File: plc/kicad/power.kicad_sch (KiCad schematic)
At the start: 67 parts, among them Q5 BSS138LT1G, Q6 CSD19537Q3, SW3 TSD003B08026A03, U11 LMR16006XDDCR, U12 TPS54560DDAR, U13 TPS26630RGER, U17 TLV76733DRVR

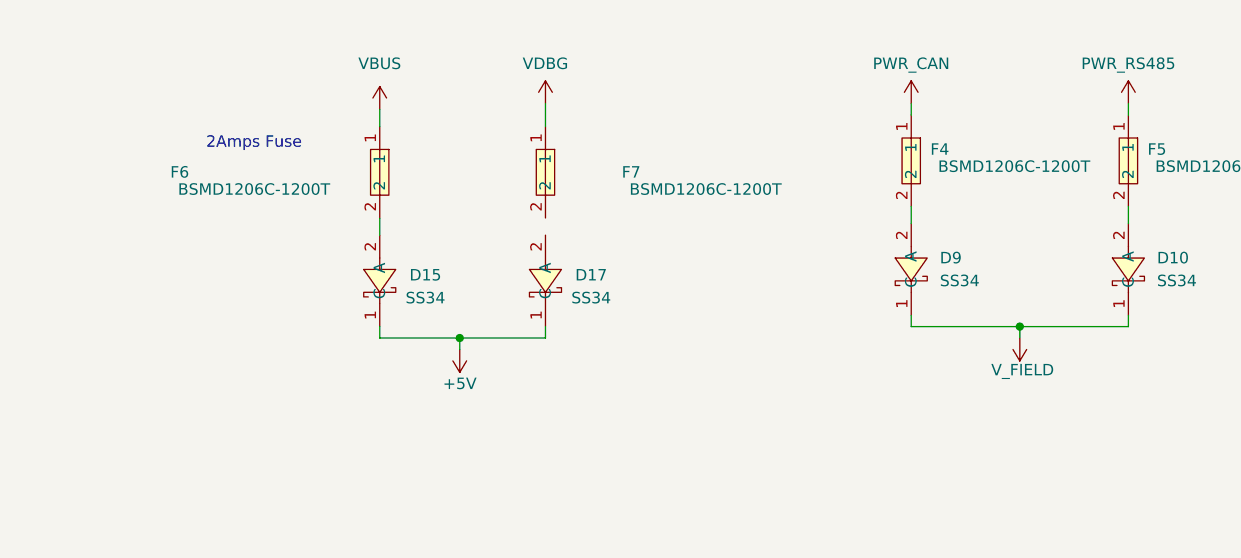
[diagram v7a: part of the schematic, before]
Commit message: AHT20 sensor added
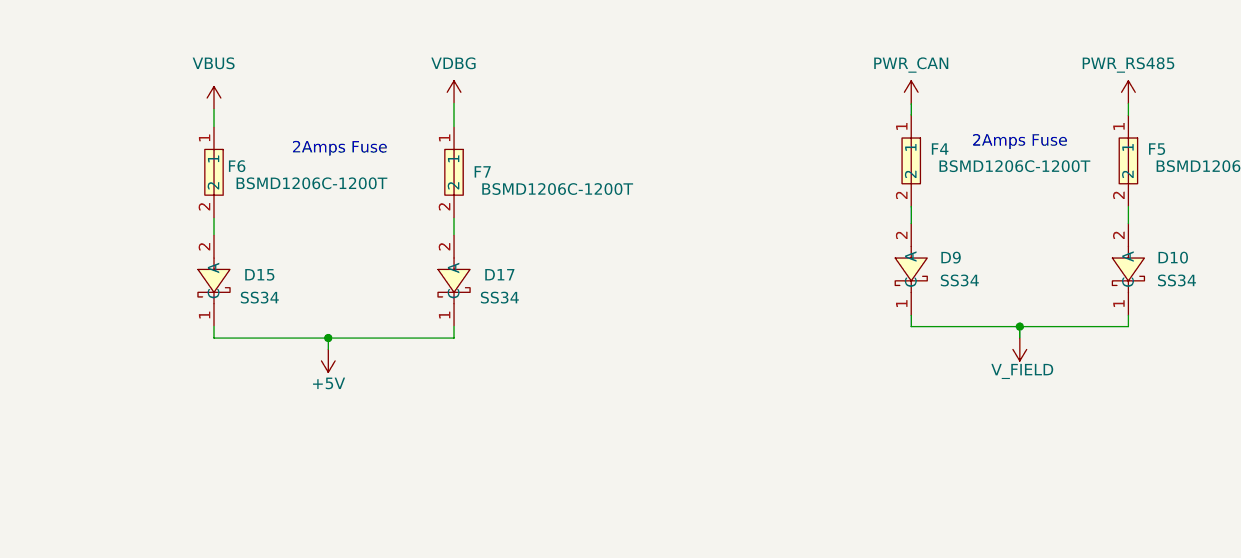
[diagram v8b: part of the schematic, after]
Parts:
- C15: footprint (none) -> Capacitor_SMD:C_0603_1608Metric
- C16, C17, C18, C19, C20, C21, C22, C23, C24, C25, C26, C27, C28, C29, C30, C31, C32, C48, C49, C50: footprint Capacitor_SMD:C_0805_2012Metric -> Capacitor_SMD:C_0603_1608Metric
- L1, L2: footprint (none) -> Inductor_SMD:L_1206_3216Metric
- R58, R59, R60, R61, R62, R63, R64, R65, R66, R67, R68, R69, R70, R71, R72, R73, R74, R75, R76, R91, R92: footprint Resistor_SMD:R_0805_2012Metric -> Resistor_SMD:R_0603_1608Metric
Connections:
- net at F7.2: now also D17.2 (A)
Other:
- moved on the sheet: D15, D17, F6, F7
